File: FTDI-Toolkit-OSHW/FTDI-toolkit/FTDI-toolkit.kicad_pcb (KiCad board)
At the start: 4 copper layers, 51.3 x 20 mm, 82 parts, among them IC1 Voltage Regulator, 2V to 5.5V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, IC10 Buffer, 74LV1T125, 1.6 V to 5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, IC11 Buffer, 74LV1T125, 1.6 V to 5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, IC12 Buffer, 74LV1T125, 1.6 V to 5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, IC13 2 NAND Gate, 4 channel, IC15 Analogue Switch, SP3T, 1 Chan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, IC2 Voltage Regulator, 2V to 5.5V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, IC3 Analogue Switch, SP3T, 1 Chan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, IC4 Buffer, 74LV1T125, 1.6 V to 5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, IC5 Buffer, 74LV1T125, 1.6 V to 5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, IC6 Buffer, 74LV1T125, 1.6 V to 5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, IC7 Buffer, 74LV1T125, 1.6 V to 5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, IC8 Dual USB-UART/FIFO, IC9 Buffer, 74LV1T125, 1.6 V to 5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, J1 Micro USB B, J2 10 Positions Header Connector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, J3 Male header, 2 x 08 pins, pit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, SW1_A Male header, 1 x 03 pins, pit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, SW1_B Male header, 1 x 03 pins, pit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, Y1 CRYSTAL, 6MHZ, 12PF, SMD,30ppm

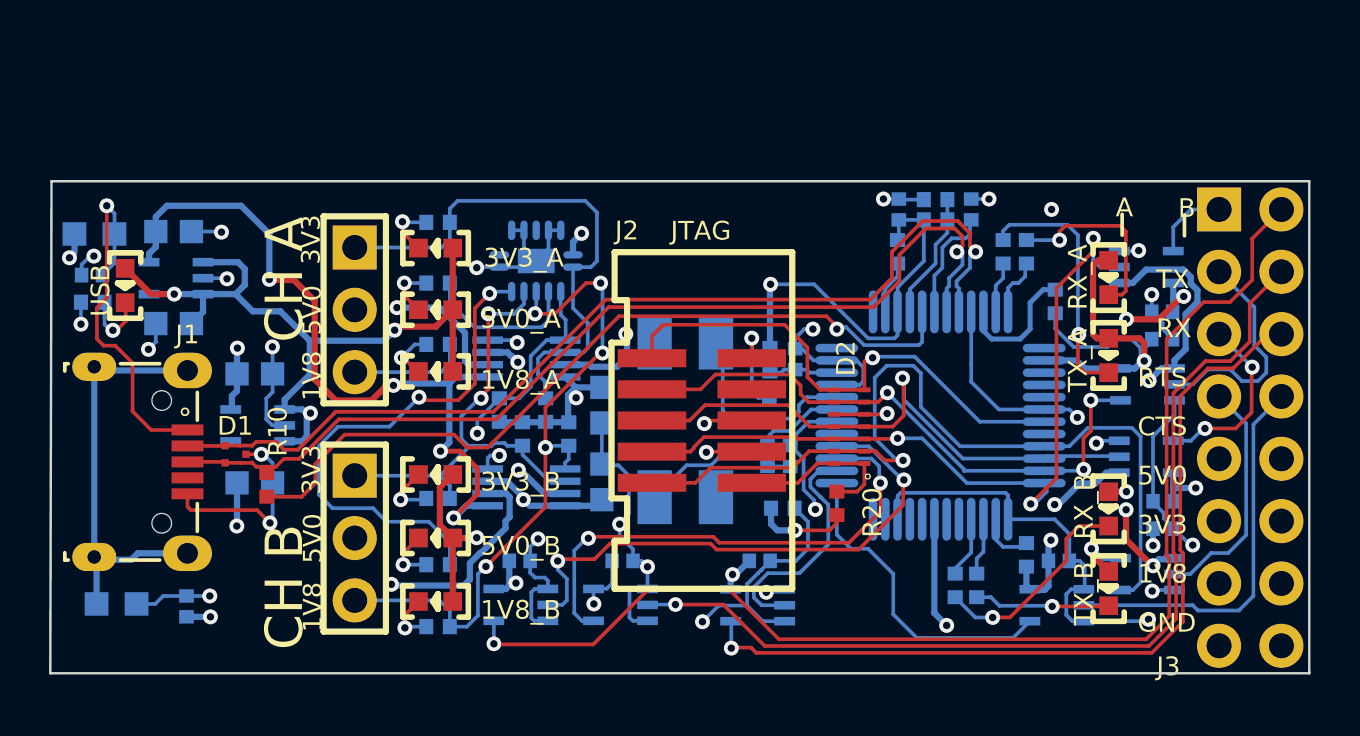
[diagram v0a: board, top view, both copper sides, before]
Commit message: PCB synced with schematic, resolved all DRCs
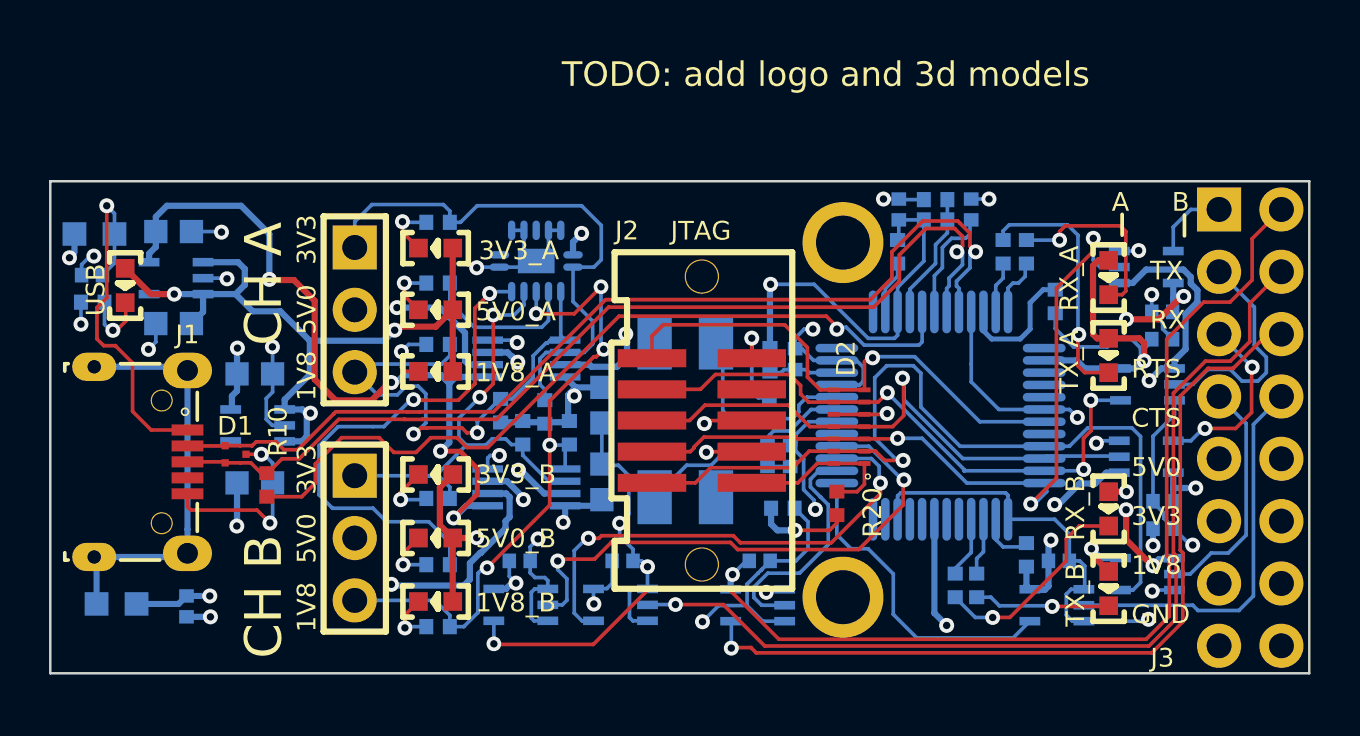
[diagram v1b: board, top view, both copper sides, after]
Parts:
- removed 1V8_A, 1V8_B, 3V3_A, 3V3_B, 5V0_A, 5V0_B, RX_A, RX_B, TX_A, TX_B, USB: LED Green 0603 case, LED0603
- removed ?: , DEFAULT
- removed SW1_A, SW1_B: Male header, 1 x 03 pins, pitch 2.54 mm, MH_1X03_2.54
- added 1V8_A1: KPT-1608SGC, LED0603, F.Cu at (144.4, -120.8)
- added 1V8_B1: KPT-1608SGC, LED0603, F.Cu at (144.4, -111.4)
- added 3V3_A1: KPT-1608SGC, LED0603, F.Cu at (144.4, -125.8)
- added 3V3_B1: KPT-1608SGC, LED0603, F.Cu at (144.4, -116.5)
- added 5V0_A1: KPT-1608SGC, LED0603, F.Cu at (144.4, -123.3)
- added 5V0_B1: KPT-1608SGC, LED0603, F.Cu at (144.4, -114.0)
- added REF**: Hole, FTDI-toolkit:Hole, F.Cu at (161.0, -111.6)
- added REF**: Hole, FTDI-toolkit:Hole, F.Cu at (161.0, -126.0)
- added RX_A1: KPT-1608SGC, LED0603, F.Cu at (171.8, -124.6)
- added RX_B1: KPT-1608SGC, LED0603, F.Cu at (171.8, -115.2)
- added SW1_A1: ~, FTDI-toolkit:MH_1X03_2.54, F.Cu at (141.1, -125.8)
- added SW1_B1: ~, FTDI-toolkit:MH_1X03_2.54, F.Cu at (141.1, -116.5)
- added TX_A1: KPT-1608SGC, LED0603, F.Cu at (171.8, -121.4)
- added TX_B1: KPT-1608SGC, LED0603, F.Cu at (171.8, -111.9)
- added USB1: ~, LED0603, F.Cu at (131.8, -124.2)
- C1, C2, C5, C6: value MLCC SMT Capacitor 1uF 0603 -> 1u
- C10, C11, C12, C13, C14, C15, C16, C19, C20, C4, C7, C8, C9: value MLCC SMT Capacitor 100nF 0402 -> C_100n_0402_16V
- C17, C18: value MLCC SMT Capacitor 27pF 0402 -> C_27p_0402
- C21, C22: value MLCC SMT Capacitor 100nF 0603 -> C_100n_0402_16V
- C3: value MLCC SMT Capacitor 10nF 0402 -> C_10n_0402
- D1: value ESD Suppressors 2-CH -> TPD2E009DRTR
- D2: value ESD Suppressors 6-CH Pass through layout -> ~
- IC1: value Voltage Regulator, 2V to 5.5V, 175mV Dropout, 3.3Vout, 200mAout -> TLV70033DCKT
- IC10, IC11, IC4, IC5, IC6, IC9: value Buffer, 74LV1T125, 1.6 V to 5.5 V, SOT-23-5 -> ~
- IC12, IC7: value Buffer, 74LV1T125, 1.6 V to 5.5 V, SOT-23-5 -> SN74LV1T125DCKR
- IC13: value 2 NAND Gate, 4 channel -> 74HC00BQ
- IC15, IC3: value Analogue Switch, SP3T, 1 Channels, 0.9 ohm, 1.65V to 5.5V, VSSOP, 8 Pins -> TS5A3359
- IC2: value Voltage Regulator, 2V to 5.5V, 175mV Dropout, 1.8Vout, 200mAout -> TLV70018DCKT
- IC8: value Dual USB-UART/FIFO -> FT2232D
- J1: value Micro USB B -> ~; footprint WE_629105150521 -> FTDI-toolkit:WE_629105150521
- J2: value 10 Positions Header Connector 0.050" (1.27mm) Surface Mount Gold -> ~; footprint SHF-105-01-X-D-SM -> FTDI-toolkit:SHF-105-01-X-D-SM
- J3: value Male header, 2 x 08 pins, pitch 2.54 mm, right angle -> ~; footprint MH_2X08_2.54_RA -> FTDI-toolkit:MH_2X08_2.54_RA
- L1, L2: value FERRITE BEAD, 0.025OHM, 3A, 0603 -> BLM18SG121TN1D
- R1, R11, R12, R14, R15, R18, R3, R6, R7, R8: value SMT Resistor 220R 0402 -> R_220R_0402
- R10: value SMT Resistor 1k54 0402 -> R_1k54_0402
- R13, R16, R17, R19, R22, R4, R5: value SMT Resistor 0402 -> R_10k_0402
- R2, R9: value SMT Resistor 470R 0402 -> R_470R_0402
- R20, R23, R24: value SMT Resistor 0402 -> R_0R_0402
- R21: value SMT Resistor 4k7 0402 -> R_4k7_0402
- Y1: value CRYSTAL, 6MHZ, 12PF, SMD,30ppm -> MQ-6.000-12-30/30/
- moved R5 0.08 mm to (148.8, -119.1)
- moved R16 0.06 mm to (149.8, -118.2)
- moved R4 0.06 mm to (147.1, -119.2)
- moved R17 0.05 mm to (147.9, -118.2)
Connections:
- net CN_JTAG_RESETN renamed /CN_JTAG_RESETn
- net FTDI_RST renamed /FTDI_RST
- net IN12_A renamed /IN12_A
- net IN12_B renamed /IN12_B
- net IN1_A renamed /IN1_A
- net IN1_B renamed /IN1_B
- net IN2_A renamed /IN2_A
- net IN2_B renamed /IN2_B
- net NetC11_1 renamed Net-(C11-Pad1)
- net NetC12_1 renamed Net-(C12-Pad1)
- net NetC17_2 renamed Net-(C17-Pad2)
- net NetC18_2 renamed Net-(C18-Pad2)
- net NetC3_1 renamed Net-(C3-Pad1)
- net NetIC8_10 renamed Net-(IC8-Pad10)
- net NetIC8_2 renamed Net-(IC8-Pad2)
- net NetIC8_26 renamed Net-(IC8-Pad26)
- net NetIC8_5 renamed Net-(IC8-Pad5)
- net SHIELD renamed GNDREF
- net UART_1_CTS renamed /UART_1_CTS
- net UART_1_CTS_T renamed /UART_1_CTS_T
- net UART_1_OE renamed /UART_1_OE
- net UART_1_RTS renamed /UART_1_RTS
- net UART_1_RTS_T renamed /UART_1_RTS_T
- net UART_1_RXD renamed /UART_1_RXD
- net UART_1_RXD_T renamed /UART_1_RXD_T
- net UART_1_RXLED renamed /UART_1_RXLED
- net UART_1_TXD renamed /UART_1_TXD
- net UART_1_TXD_T renamed /UART_1_TXD_T
- net UART_1_TXLED renamed /UART_1_TXLED
- net UART_2_CTS renamed /UART_2_CTS
- net UART_2_CTS_T renamed /UART_2_CTS_T
- net UART_2_RTS renamed /UART_2_RTS
- net UART_2_RTS_T renamed /UART_2_RTS_T
- net UART_2_RXD renamed /UART_2_RXD
- net UART_2_RXD_T renamed /UART_2_RXD_T
- net UART_2_RXLED renamed /UART_2_RXLED
- net UART_2_TXD renamed /UART_2_TXD
- net UART_2_TXD_T renamed /UART_2_TXD_T
- net UART_2_TXLED renamed /UART_2_TXLED
- net USB_D_N renamed /USB_D_N
- net USB_D_P renamed /USB_D_P
- IC13 pad 11: (no net) -> Net-(IC13-Pad11)
- IC13 pad 8: (no net) -> Net-(IC13-Pad8)
- IC8 pad 1: (no net) -> Net-(IC8-Pad1)
- IC8 pad 13: (no net) -> Net-(IC8-Pad13)
- IC8 pad 15: (no net) -> Net-(IC8-Pad15)
- IC8 pad 16: (no net) -> Net-(IC8-Pad16)
- IC8 pad 17: (no net) -> Net-(IC8-Pad17)
- IC8 pad 20: (no net) -> Net-(IC8-Pad20)
- IC8 pad 29: (no net) -> Net-(IC8-Pad29)
- IC8 pad 30: (no net) -> Net-(IC8-Pad30)
- IC8 pad 32: (no net) -> Net-(IC8-Pad32)
- IC8 pad 33: (no net) -> Net-(IC8-Pad33)
- IC8 pad 35: (no net) -> Net-(IC8-Pad35)
- IC8 pad 36: (no net) -> Net-(IC8-Pad36)
- IC8 pad 41: (no net) -> Net-(IC8-Pad41)
- IC8 pad 48: (no net) -> Net-(IC8-Pad48)
- J1 pad 4: (no net) -> Net-(J1-Pad4)
- J2 pad 7: (no net) -> Net-(J2-Pad7)
- R1 pad 1: Net3V3_A_K -> Net-(3V3_A1-PadK)
- R11 pad 2: NetR11_2 -> Net-(R11-Pad2)
- R12 pad 2: NetR12_2 -> Net-(R12-Pad2)
- R14 pad 2: NetR14_2 -> Net-(R14-Pad2)
- R15 pad 2: NetR15_2 -> Net-(R15-Pad2)
- R18 pad 1: Net5V0_B_K -> Net-(5V0_B1-PadK)
- R2 pad 2: NetR2_2 -> Net-(R2-Pad2)
- R3 pad 1: Net1V8_A_K -> Net-(1V8_A1-PadK)
- R6 pad 1: Net5V0_A_K -> Net-(5V0_A1-PadK)
- R7 pad 1: Net3V3_B_K -> Net-(3V3_B1-PadK)
- R8 pad 1: Net1V8_B_K -> Net-(1V8_B1-PadK)
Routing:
- net Net1: track 142.7 -> 0.00 mm
- net NetR11_2: track 10.5 -> 0.00 mm, vias 1 -> 0
- net Net-(R11-Pad2): track 0.00 -> 10.5 mm, vias 0 -> 1
- net Net-(R15-Pad2): track 0.00 -> 8.67 mm, vias 0 -> 1
- net NetR15_2: track 8.67 -> 0.00 mm, vias 1 -> 0
- net NetR12_2: track 7.78 -> 0.00 mm, vias 1 -> 0
- net Net-(R12-Pad2): track 0.00 -> 7.78 mm, vias 0 -> 1
- net NetR14_2: track 5.54 -> 0.00 mm, vias 1 -> 0
- net Net-(R14-Pad2): track 0.00 -> 5.54 mm, vias 0 -> 1
- net NetR2_2: track 2.79 -> 0.00 mm, vias 1 -> 0
- net Net-(R2-Pad2): track 0.00 -> 2.79 mm, vias 0 -> 1
- net Net-(1V8_A1-PadK): track 0.00 -> 2.54 mm, vias 0 -> 1
- net Net3V3_B_K: track 2.41 -> 0.00 mm, vias 1 -> 0
- net Net-(3V3_B1-PadK): track 0.00 -> 2.41 mm, vias 0 -> 1
- net Net3V3_A_K: track 2.33 -> 0.00 mm, vias 1 -> 0
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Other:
- outline, holes or cut-outs redrawn
- net class Default: via_dia 0.61 -> 0.6
- rule via_min_size: 0.61 -> 0.6
- board text added: "TODO: add logo and 3d models"
